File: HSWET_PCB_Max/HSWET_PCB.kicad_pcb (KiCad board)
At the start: 2 copper layers, 138.5 x 86 mm, 42 parts, among them IC3 PS2565L-1-V-F3-A, IC4 PS2565L-1-V-F3-A, IC5 PS2565L-1-V-F3-A, J1 CON-SOCJ-2155, J10 arduino enc, J11 turbine pwr, J2 emergency stop, J3 CON-SOCJ-2155, J4 turbine bus, J5 5v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

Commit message: bruh
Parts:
- removed REF** (x4): MountingHole_3.2mm_M3, MountingHole:MountingHole_3.2mm_M3
- added J12: XT30_POWER_IN, Connector_AMASS:AMASS_XT30PW-M_1x02_P2.50mm_Horizontal, F.Cu at (192.0, 59.5)
- moved J3 1.80 mm to (168.0, 58.5)

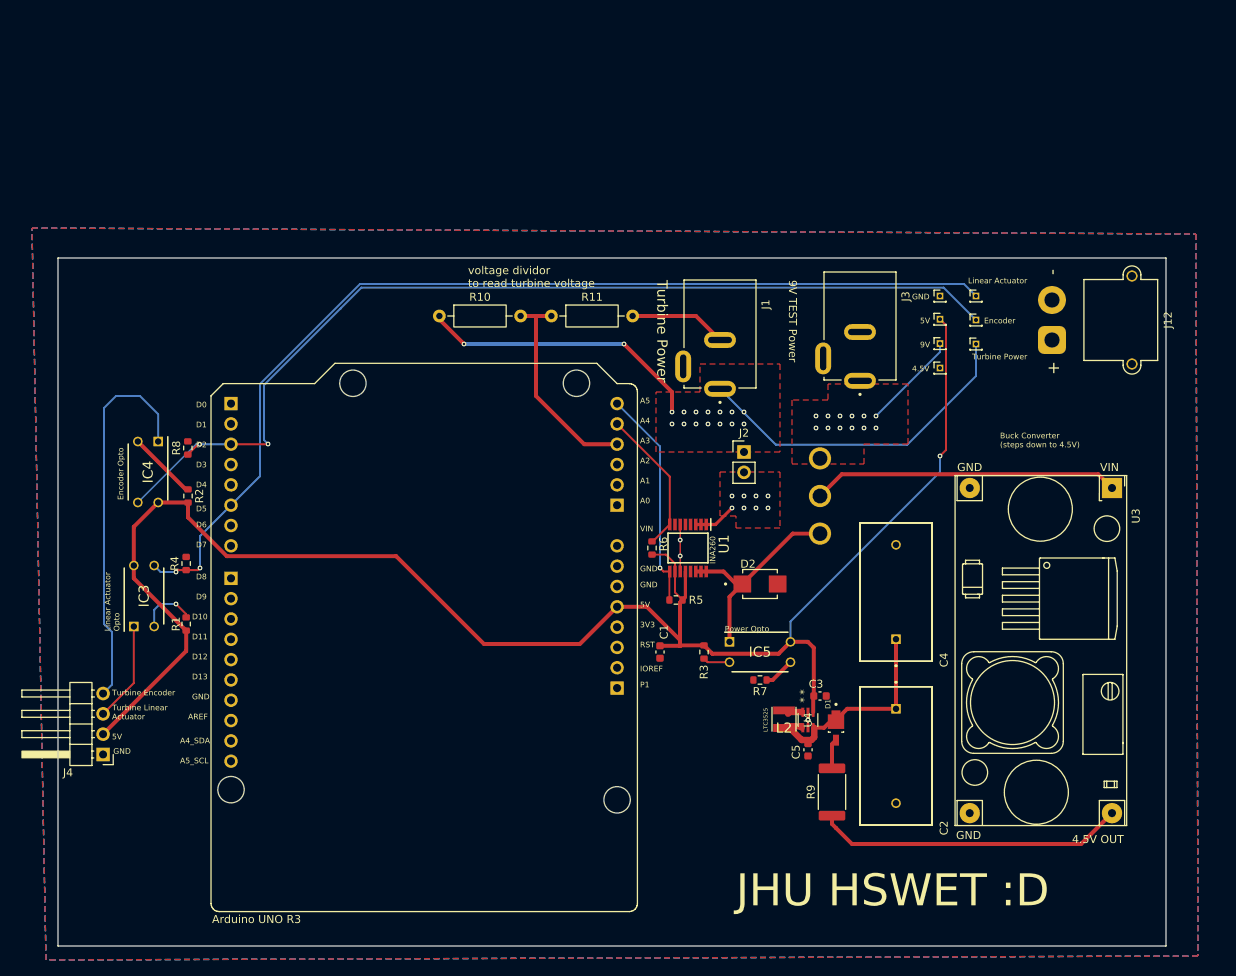
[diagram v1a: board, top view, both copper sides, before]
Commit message: made traces for power muuuuuuuuuuuuch bigger and added connector for load and removed 9v stuff just plug into the turbine
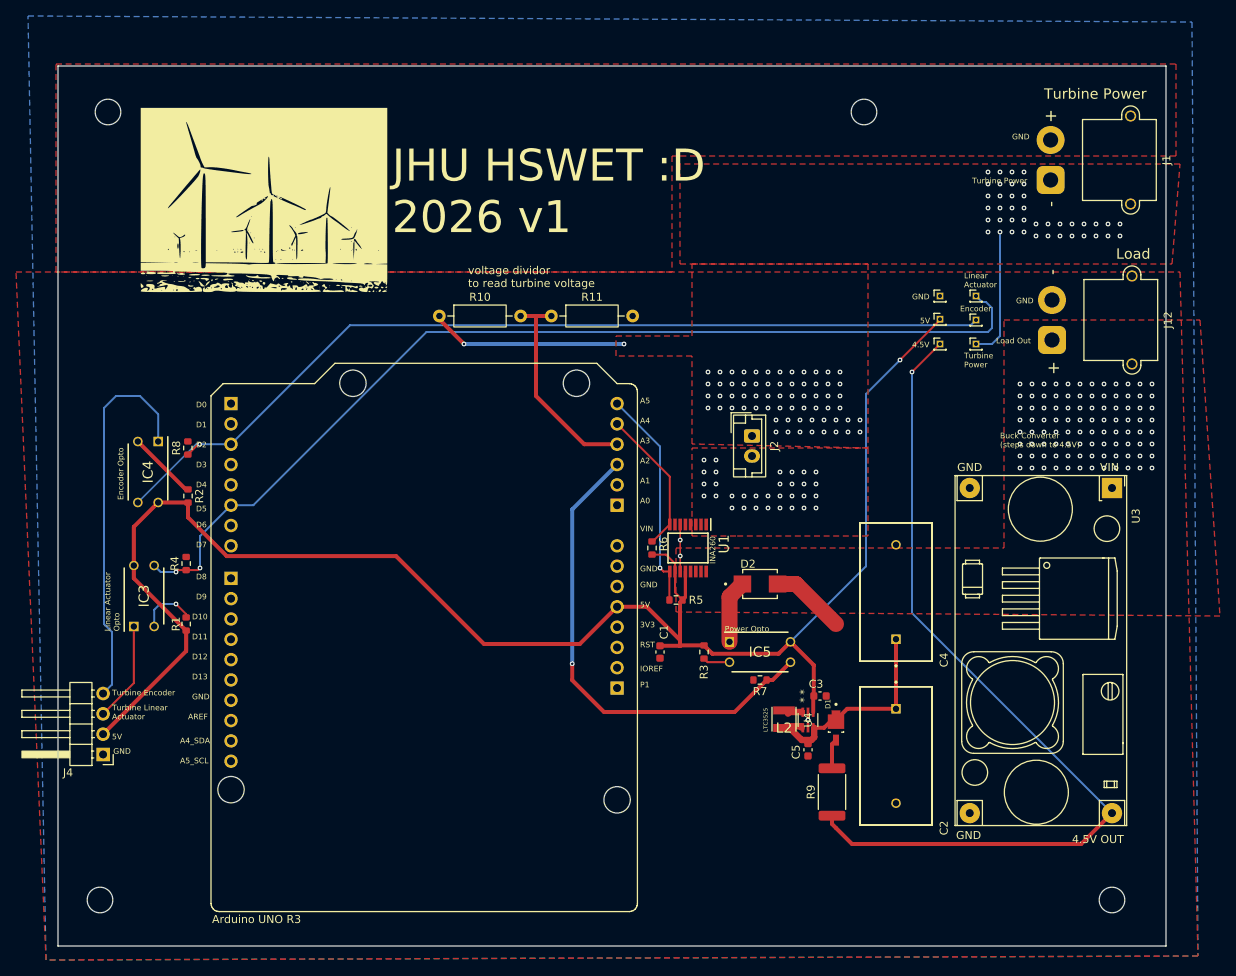
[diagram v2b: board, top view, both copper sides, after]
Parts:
- removed J3: CON-SOCJ-2155, footprints:GRAVITECH_CON-SOCJ-2155
- removed J6: 9v, Connector_PinHeader_1.00mm:PinHeader_1x01_P1.00mm_Vertical
- removed S1: 100SP1T1B4M2QE, footprints:100SP1T1B4M2QE
- added G***: LOGO, LOGO, F.Cu at (93.5, 42.0)
- added REF**: MountingHole_3.2mm_M3, MountingHole:MountingHole_3.2mm_M3, F.Cu at (73.0, 129.5)
- added REF**: MountingHole_3.2mm_M3, MountingHole:MountingHole_3.2mm_M3, F.Cu at (168.5, 31.0)
- added REF**: MountingHole_3.2mm_M3, MountingHole:MountingHole_3.2mm_M3, F.Cu at (199.5, 129.5)
- added REF**: MountingHole_3.2mm_M3, MountingHole:MountingHole_3.2mm_M3, F.Cu at (74.0, 31.0)
- J1: value CON-SOCJ-2155 -> TURBINE_IN; footprint footprints:GRAVITECH_CON-SOCJ-2155 -> Connector_AMASS:AMASS_XT30PW-M_1x02_P2.50mm_Horizontal
- J12: value XT30_POWER_IN -> LOAD_OUT
- J2: footprint Connector_PinHeader_2.54mm:PinHeader_1x02_P2.54mm_Vertical -> Connector_JST:JST_EH_B2B-EH-A_1x02_P2.50mm_Vertical
- moved J1 45.9 mm to (191.8, 39.5)
- moved J7 3.00 mm to (178.0, 60.0)
- moved J2 2.24 mm to (154.5, 71.5), turned to -90 degrees
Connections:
- A1 pad A2: unconnected-(A1-PadA2) -> Sensor_PWR
- J1 pad 2: unconnected-(J1-Pad2) -> GND
- J12 pad 1: Turbine_PWR -> Turbine_PWR_Sensed
- J7 pad 1: 4.5V -> 4.5V_BUCK
- U3 pad 1: Net-(U3-Vin) -> Turbine_PWR_Sensed
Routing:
- net 4.5V_BUCK: track 38.7 -> 109.1 mm, vias 0 -> 1
- net Sensor_PWR: track 3.91 -> 60.8 mm, vias 0 -> 1
- net Net-(U3-Vin): track 38.3 -> 0.00 mm
- net Turbine_PWR: track 78.2 -> 41.2 mm, vias 16 -> 106
- net Turbine_PWR_Sensed: track 26.7 -> 8.69 mm, vias 0 -> 96
- net 9V: track 12.4 -> 0.00 mm, vias 12 -> 0
- net arduino_encoder: track 124.9 -> 116.5 mm, vias 2 -> 1
- net Turbine_PWR_Safety: track 5.38 -> 0.00 mm, vias 8 -> 32
- net GND: track 20.0 -> 17.2 mm
- net arduino_lin_act: track 127.7 -> 125.1 mm
- net 5V: track 210.5 -> 208.6 mm
- added copper zone on F.Cu, net Turbine_PWR_Sensed
- removed copper zone on B.Cu, net 5V
- removed copper zone on F.Cu, net 9V
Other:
- board size 138.5 x 86 mm -> 138.5 x 110 mm
- board text added: "JHU HSWET :D 2026 v1"
- board text added: "Load"
- board text added: "Load Out"
- board text removed: "9V"
- board text removed: "9V TEST Power"
- board text removed: "JHU HSWET :D"

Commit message: fixed lin act schematci
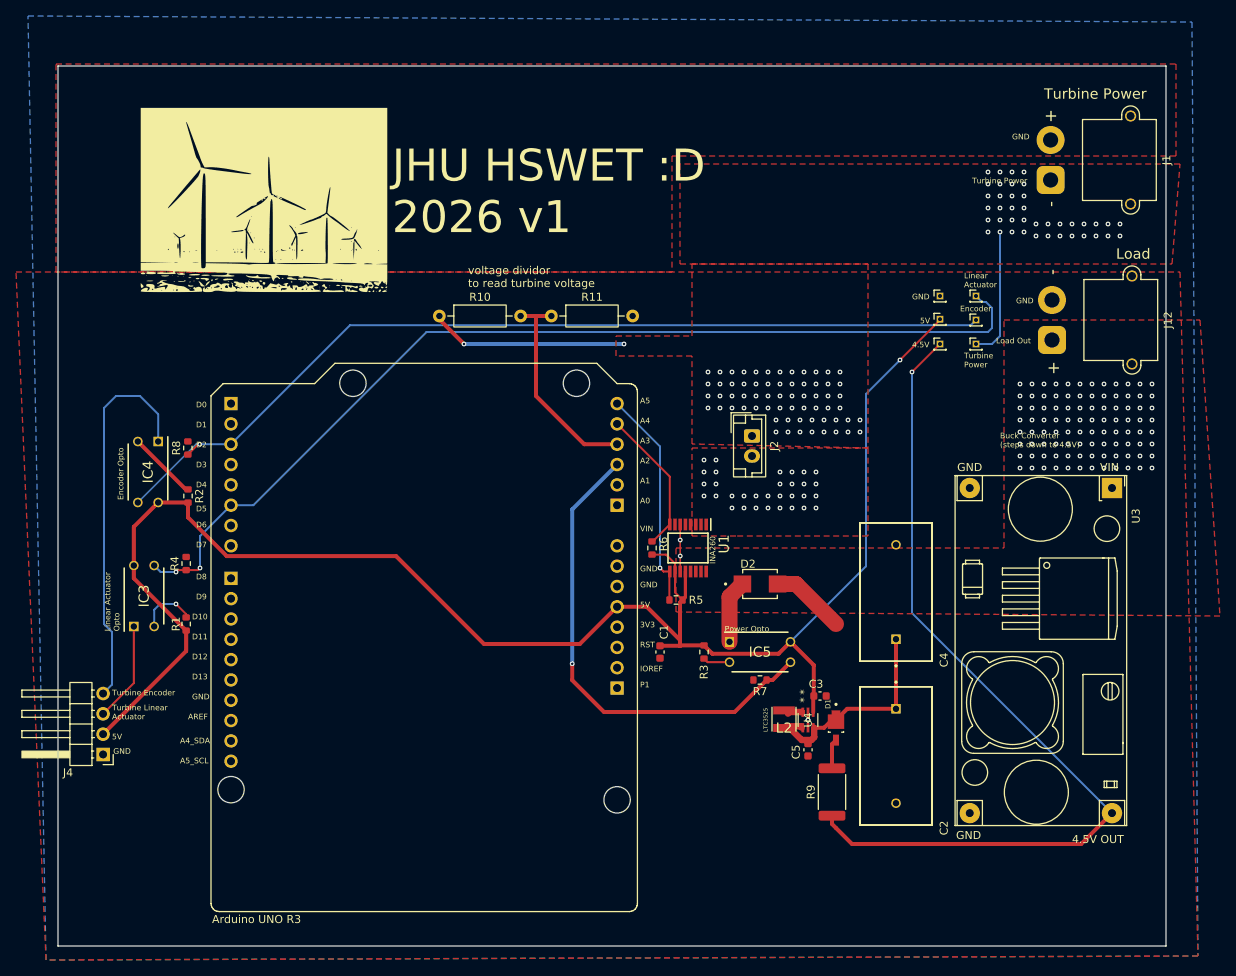
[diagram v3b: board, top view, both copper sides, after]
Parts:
- removed REF** (x4): MountingHole_3.2mm_M3, MountingHole:MountingHole_3.2mm_M3
